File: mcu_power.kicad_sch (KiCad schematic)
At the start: 36 parts, among them U1 MIMXRT1052CVJ5B, Y1 DSC1001BI5-024.0000, Y2 830107834801

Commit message: v0.2
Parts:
- added C53: 10uF, symbol Device:C_Small
- added C54: 22uF, symbol Device:C_Small
- added L4: 2.2uH, symbol Device:L
- added R13: 100k, symbol Device:R_Small_US
- added U10: TPS62162DSG, Package_SON:WSON-8-1EP_2x2mm_P0.5mm_EP0.9x1.6mm_ThermalVias, symbol Regulator_Switching:TPS62162DSG
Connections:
- net +3.3V: now also C54.1, L4.2, R13.1, U10.6 (VOS)
- net DCDC_IN: no longer U1.J5 (DCDC_SENSE)
- net DCDC_OUT: now also U1.J5 (DCDC_SENSE)
- net GND: now also C53.2, C54.2, U10.1 (PGND), U10.4 (AGND), U10.5 (FB), U10.9 (PAD)
- net PMIC_ON_REQ: now also U10.3 (EN)
- net ONOFF: no longer names the net of U1.M6 (ONOFF)
- net PMIC_STBY_REQ: no longer names the net of U1.L7 (PMIC_STBY_REQ)
- net RESET renamed ~{RESET}
- new net: R13.2, U10.8 (PG)
- new net: L4.1, U10.7 (SW)
- new net +5V: C53.1, U10.2 (VIN)
- no-connect marks 5 -> 7
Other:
- title: RT1050 DevBoard for Project Horizon -> Payload Board for Pleiades Atlas

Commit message: started layout
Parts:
- C53: footprint (none) -> Capacitor_SMD:C_0402_1005Metric
- C54: footprint (none) -> Capacitor_SMD:C_0603_1608Metric
- L4, R13: footprint (none) -> Resistor_SMD:R_0402_1005Metric
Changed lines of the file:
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@@
 	(wire
 		(pts
+			(xy 41.91 204.47) (xy 45.72 204.47)
+		)
+		(stroke
+			(width 0)
+			(type default)
+		)
+	)
+	(wire
+		(pts
 			(xy 238.76 35.56) (xy 250.19 35.56)
 		)
@@
 		)
 	)
-	(global_label "PG_3V3"
-		(shape input)
-		(at 45.72 204.47 180)
-		(effects
-			(font
-				(size 1.27 1.27)
-			)
-			(justify right)
-		)
-		(property "Intersheetrefs" "${INTERSHEET_REFS}"
-			(at 45.72 204.47 0)
-			(effects
-				(font
-					(size 1.27 1.27)
-				)
-				(hide yes)
-			)
-		)
-	)
 	(global_label "PMIC_ON_REQ"
 		(shape bidirectional)
@@
 		)
 	)
-	(global_label "PG_3V3"
-		(shape input)
-		(at 78.74 196.85 270)
-		(effects
-			(font
-				(size 1.27 1.27)
-			)
-			(justify right)
-		)
-		(property "Intersheetrefs" "${INTERSHEET_REFS}"
-			(at 78.74 196.85 90)
-			(effects
-				(font
-					(size 1.27 1.27)
-				)
-				(hide yes)
-			)
-		)
-	)
 	(global_label "PMIC_ON_REQ"
 		(shape bidirectional)
@@
 	)
 	(symbol
+		(lib_id "power:+3.3V")
+		(at 41.91 204.47 0)
+		(unit 1)
+		(exclude_from_sim no)
+		(in_bom yes)
+		(on_board yes)
+		(dnp no)
+		(fields_autoplaced yes)
+		(property "Reference" "#PWR0130"
+			(at 41.91 208.28 0)
+			(effects
+				(font
+					(size 1.27 1.27)
+				)
+				(hide yes)
+			)
+		)
+		(property "Value" "+3.3V"
+			(at 41.91 199.39 0)
+			(effects
+				(font
+					(size 1.27 1.27)
+				)
+			)
+		)
+		(property "Footprint" ""
+			(at 41.91 204.47 0)
+			(effects
+				(font
+					(size 1.27 1.27)
+				)
+				(hide yes)
+			)
+		)
+		(property "Datasheet" ""
+			(at 41.91 204.47 0)
+			(effects
+				(font
+					(size 1.27 1.27)
+				)
+				(hide yes)
+			)
+		)
+		(property "Description" "Power symbol creates a global label with name \"+3.3V\""
+			(at 41.91 204.47 0)
+			(effects
+				(font
+					(size 1.27 1.27)
+				)
+				(hide yes)
+			)
+		)
+		(pin "1"
+		)
+		(instances
+			(project "RT1050"
+				(path "/dd9d031d-43a1-4442-b493-27451a14e0d9/ef9a9590-bc2d-4a19-b722-cc119a748157"
+					(reference "#PWR0130")
+					(unit 1)
+				)
+			)
+		)
+	)
+	(symbol
 		(lib_id "MIMXRT1052CVJ5B:MIMXRT1052CVJ5B")
 		(at 85.09 109.22 0)
@@
 			)
 		)
-		(property "Footprint" ""
+		(property "Footprint" "Resistor_SMD:R_0402_1005Metric"
 			(at 48.26 204.47 0)
 			(effects
@@
 			)
 		)
-		(property "Footprint" ""
+		(property "Footprint" "Capacitor_SMD:C_0603_1608Metric"
 			(at 85.09 196.85 0)
 			(effects
@@
 			)
 		)
-		(property "Footprint" ""
+		(property "Footprint" "Resistor_SMD:R_0402_1005Metric"
 			(at 74.93 194.31 0)
 			(effects
@@
 			)
 		)
-		(property "Footprint" ""
+		(property "Footprint" "Capacitor_SMD:C_0402_1005Metric"
 			(at 30.48 196.85 0)
 			(effects

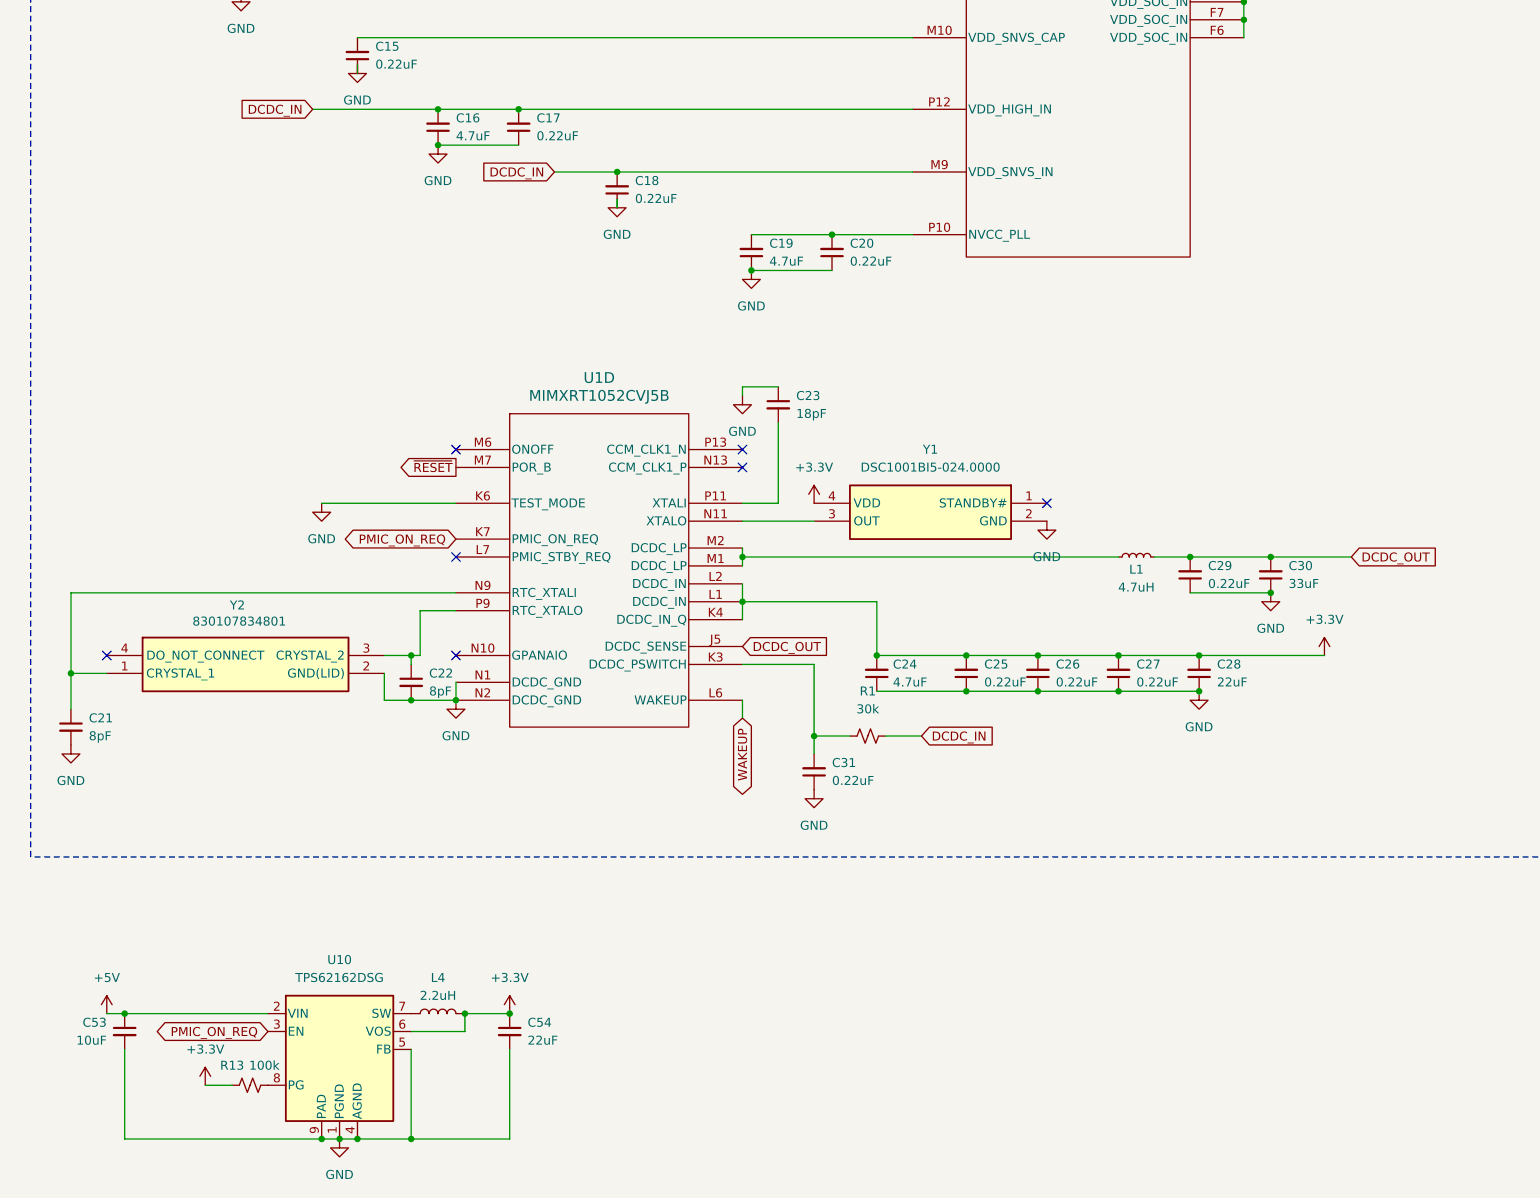
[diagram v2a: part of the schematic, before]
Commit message: redid power rails to allow for sleep
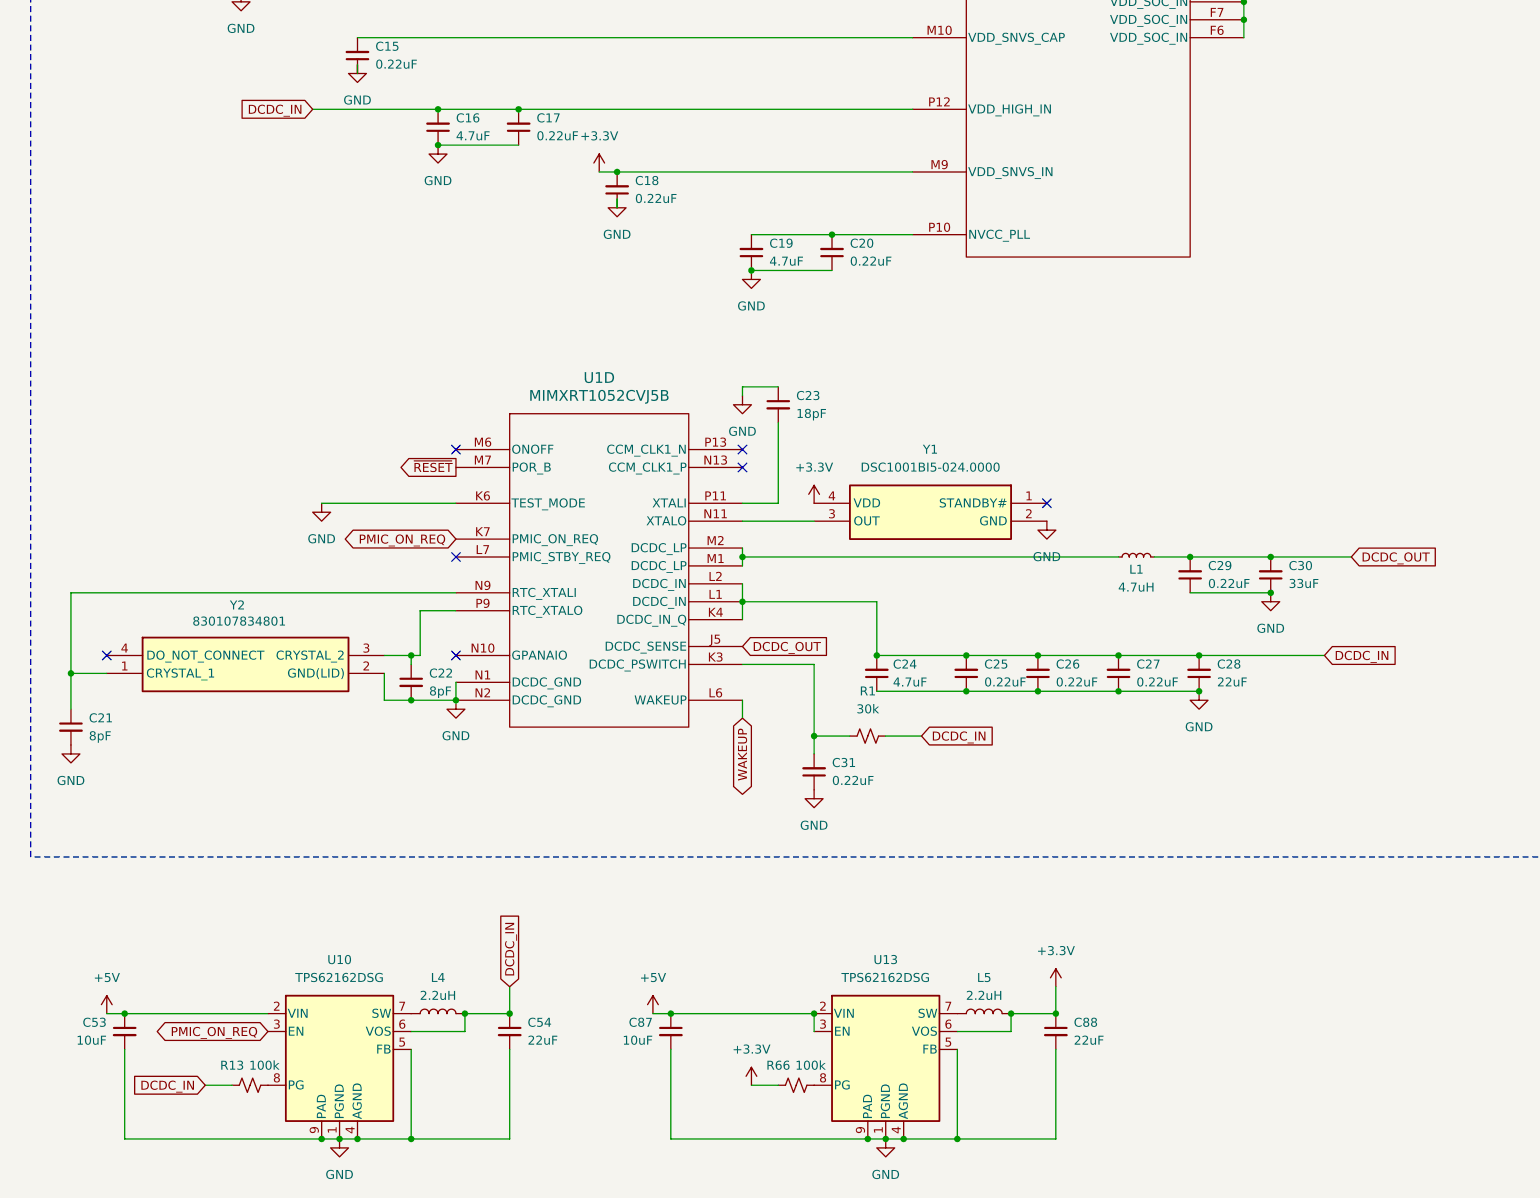
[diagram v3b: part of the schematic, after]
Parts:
- added C87: 10uF, Capacitor_SMD:C_0402_1005Metric, symbol Device:C_Small
- added C88: 22uF, Capacitor_SMD:C_0603_1608Metric, symbol Device:C_Small
- added L5: 2.2uH, Resistor_SMD:R_0402_1005Metric, symbol Device:L
- added R66: 100k, Resistor_SMD:R_0402_1005Metric, symbol Device:R_Small_US
- added U13: TPS62162DSG, Package_SON:WSON-8-1EP_2x2mm_P0.5mm_EP0.9x1.6mm_ThermalVias, symbol Regulator_Switching:TPS62162DSG
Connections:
- net +3.3V: now also C18.2, U1.M9 (VDD_SNVS_IN), C88.1, L5.2, R66.1, U13.6 (VOS); no longer C24.2, C25.2, C26.2, C27.2, C28.2, C54.1, L4.2, R13.1, U1.K4 (DCDC_IN_Q), U1.L1 (DCDC_IN), U1.L2 (DCDC_IN), U10.6 (VOS)
- net +5V: now also C87.1, U13.2 (VIN), U13.3 (EN)
- net DCDC_IN: now also C24.2, C25.2, C26.2, C27.2, C28.2, C54.1, L4.2, R13.1, U1.K4 (DCDC_IN_Q), U1.L1 (DCDC_IN), U1.L2 (DCDC_IN), U10.6 (VOS); no longer C18.2, U1.M9 (VDD_SNVS_IN)
- net GND: now also C87.2, C88.2, U13.1 (PGND), U13.4 (AGND), U13.5 (FB), U13.9 (PAD)
- new net: L5.1, U13.7 (SW)
- new net: R66.2, U13.8 (PG)

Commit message: finished layout of v0.2!
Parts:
- removed C53: 10uF, Capacitor_SMD:C_0402_1005Metric, symbol Device:C_Small
- removed C54: 22uF, Capacitor_SMD:C_0603_1608Metric, symbol Device:C_Small
- removed L4: 2.2uH, Resistor_SMD:R_0402_1005Metric, symbol Device:L
- removed R13: 100k, Resistor_SMD:R_0402_1005Metric, symbol Device:R_Small_US
- removed U10: TPS62162DSG, Package_SON:WSON-8-1EP_2x2mm_P0.5mm_EP0.9x1.6mm_ThermalVias, symbol Regulator_Switching:TPS62162DSG
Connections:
- net DCDC_IN is gone; now on net +3.3V: C13.2, C14.2, C16.2, C17.2, C24.2, C25.2, C26.2, C27.2, C28.2, R1.2, U1.K4 (DCDC_IN_Q), U1.L1 (DCDC_IN), U1.L2 (DCDC_IN), U1.N14 (VDDA_ADC_3P3), U1.P12 (VDD_HIGH_IN)
